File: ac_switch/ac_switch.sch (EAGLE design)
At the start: 23 parts, among them IC1 TINY85, T1 BC337

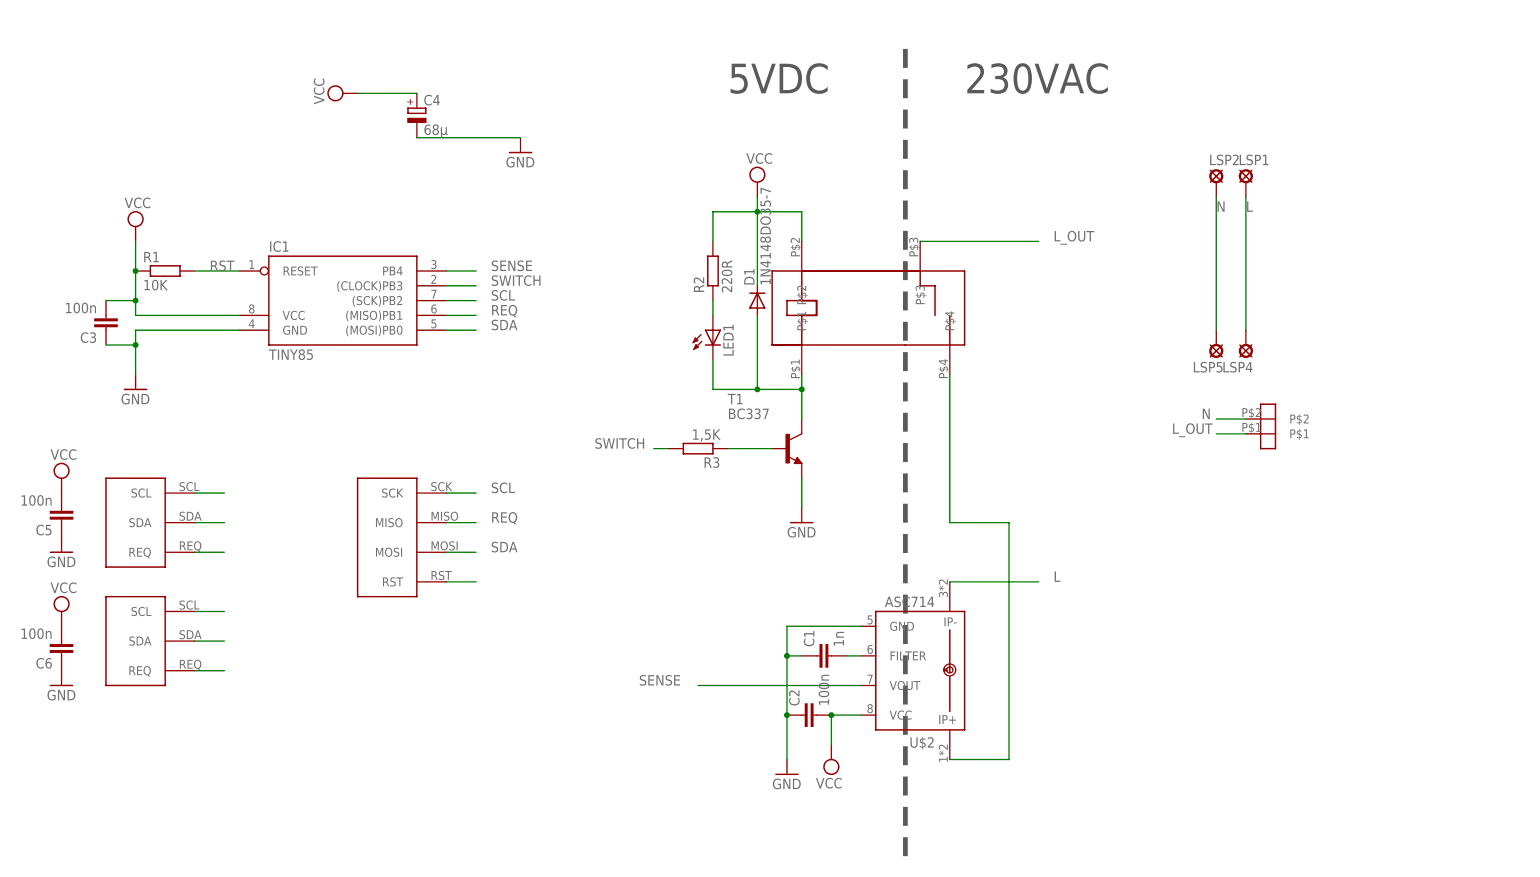
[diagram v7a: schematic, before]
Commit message: AC switch: re-routing
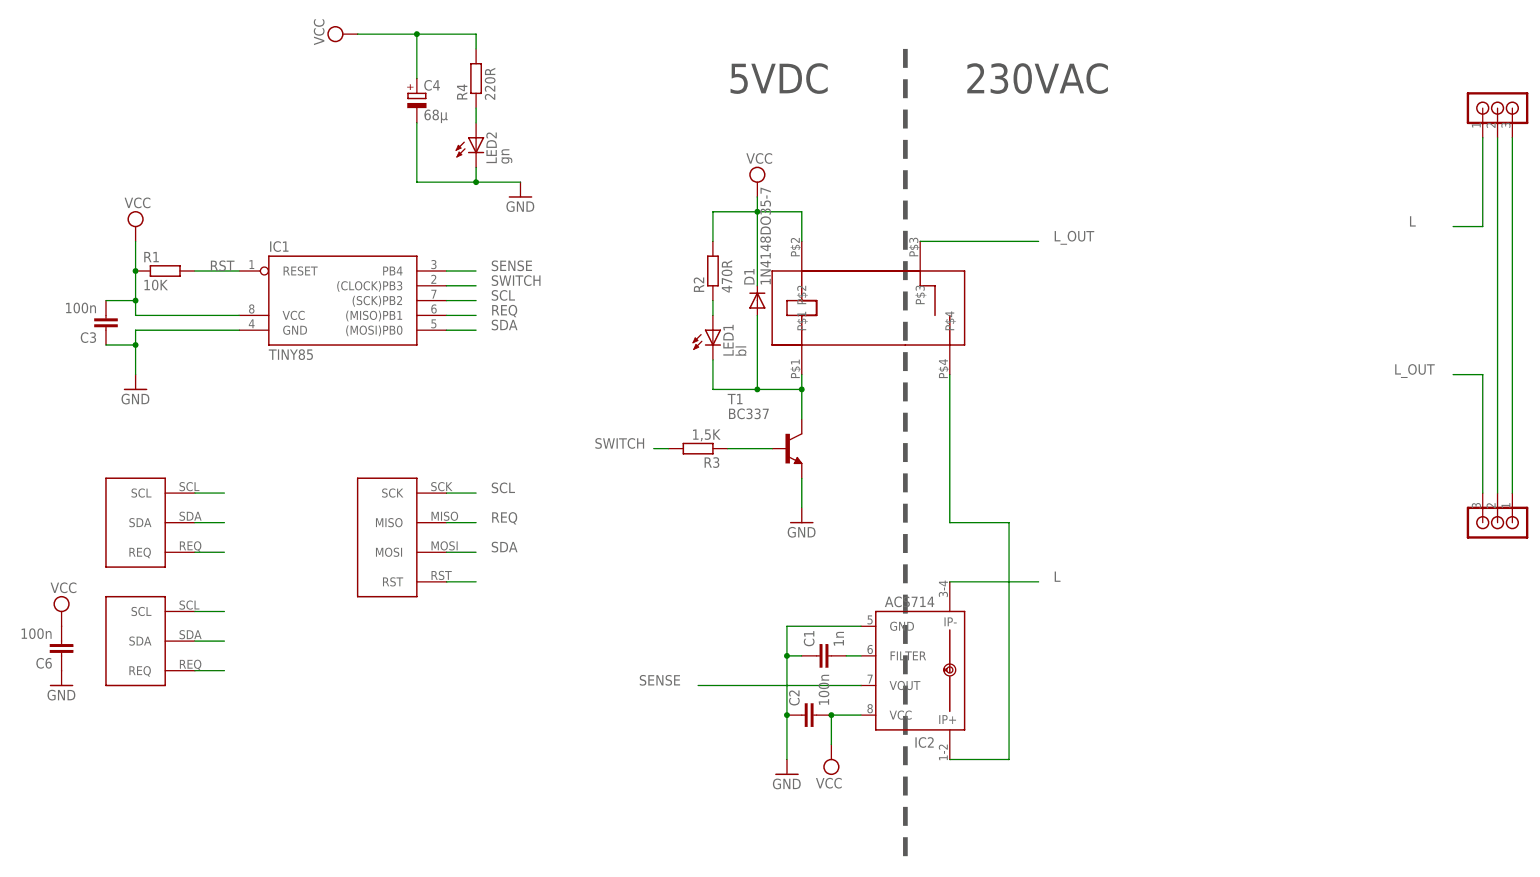
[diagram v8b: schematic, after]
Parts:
- removed C5: 100n, resistor:C-EU025-024X044
- removed LSP1, LSP2, LSP4, LSP5: SE14, solpad:SE14
- added IC2: ACS714, n39:ACS714
- added LED2: gn, led:LED3MM
- added R4: 220R, resistor:R-EU_0207/10
- LED1: value (none) -> bl
- R1: device resistor:R-EU_0207/10 -> resistor:R-EU_0207/12
- R2: value 220R -> 470R; device resistor:R-EU_0204/7 -> resistor:R-EU_0207/10
- R3: device resistor:R-EU_0204/7 -> resistor:R-EU_0207/10
- U$2: value ASC714 -> RIACON_101_3; device n39:ASC714 -> n39:RIACON_101_3
- U$6: value WAGO_734_262 -> RIACON_101_3; device n39:WAGO_734_262 -> n39:RIACON_101_3
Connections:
- removed net N: LSP2.MP, LSP5.MP, U$6.P$2
- new net N$6: LED2.A, R4.1
- new net N$8: U$2.3, U$6.1
- new net N$9: U$2.2, U$6.2
- net GND: now also IC2.GND, LED2.C; no longer C5.1, U$2.GND
- net L: now also IC2.IP-, U$2.1; no longer LSP1.MP, LSP4.MP, U$2.IP-
- net L_OUT: now also U$6.3; no longer U$6.P$1
- net N$2: now also IC2.FILTER; no longer U$2.FILTER
- net N$3: now also IC2.IP+; no longer U$2.IP+
- net SENSE: now also IC2.VOUT; no longer U$2.VOUT
- net VCC: now also IC2.VCC, R4.2; no longer C5.2, U$2.VCC
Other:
- moved on the sheet: C4
